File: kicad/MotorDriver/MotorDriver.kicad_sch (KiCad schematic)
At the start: 75 parts, among them J1 Conn_01x02_Socket, J2 Conn_01x03_Socket, U1 DRV8323RSRGZR, U2 CSD88599Q5DC, U3 CSD88599Q5DC, U5 CSD88599Q5DC, U6 STM32G474RETx

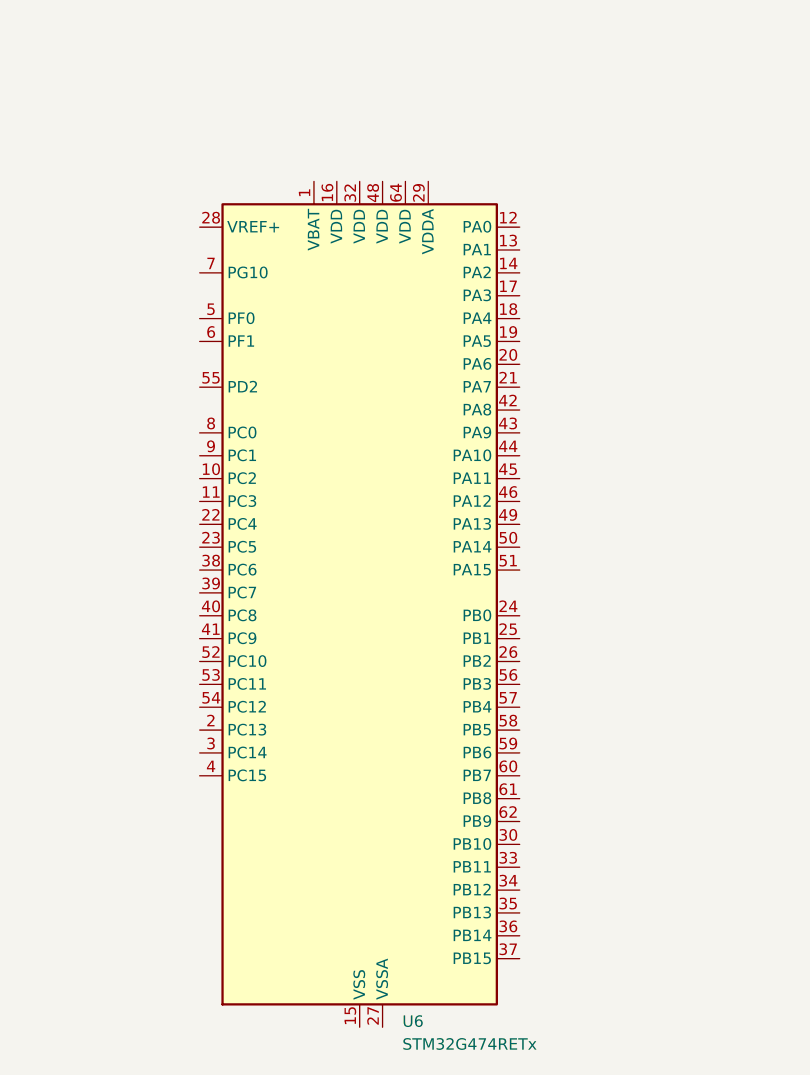
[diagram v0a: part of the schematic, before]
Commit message: Good progress on the leg prototype. Looking at the jacobian project again, i think I can use some stuff from that project to help size the link lengths and also something to relate the tip forces to joint torques
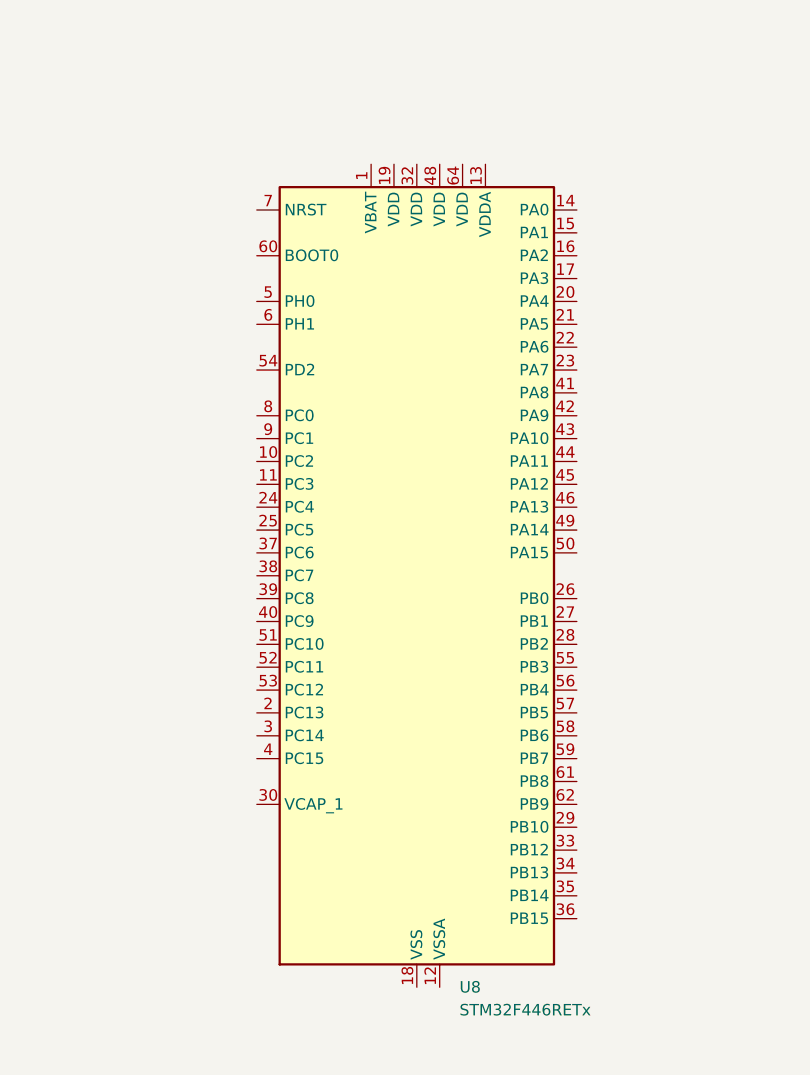
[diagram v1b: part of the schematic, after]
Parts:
- removed U6: STM32G474RETx, Package_QFP:LQFP-64_10x10mm_P0.5mm, symbol MCU_ST_STM32G4:STM32G474RETx
- added U8: STM32F446RETx, Package_QFP:LQFP-64_10x10mm_P0.5mm, symbol MCU_ST_STM32F4:STM32F446RETx
- L1: footprint (none) -> Inductor_SMD:L_0603_1608Metric
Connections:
- new net: U8.18 (VSS), U8.31 (VSS), U8.47 (VSS), U8.63 (VSS)
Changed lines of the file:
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@@
     (effects (font (size 1.27 1.27)) (justify left bottom))
+  )
+  (symbol (lib_id "MCU_ST_STM32F4:STM32F446RETx") (at 100.33 288.29 0) (unit 1)
+    (in_bom yes) (on_board yes) (dnp no) (fields_autoplaced)
+    (property "Reference" "U8" (at 105.0641 334.01 0)
+      (effects (font (size 1.27 1.27)) (justify left))
+    )
+    (property "Value" "STM32F446RETx" (at 105.0641 336.55 0)
+      (effects (font (size 1.27 1.27)) (justify left))
+    )
+    (property "Footprint" "Package_QFP:LQFP-64_10x10mm_P0.5mm" (at 85.09 331.47 0)
+      (effects (font (size 1.27 1.27)) (justify right) hide)
+    )
+    (property "Datasheet" "https://www.st.com/resource/en/datasheet/stm32f446re.pdf" (at 100.33 288.29 0)
+      (effects (font (size 1.27 1.27)) hide)
+    )
+    (pin "10")
+    (pin "30")
+    (pin "35")
+    (pin "2")
+    (pin "26")
+    (pin "23")
+    (pin "29")
+    (pin "27")
+    (pin "52")
+    (pin "31")
+    (pin "53")
+    (pin "58")
+    (pin "38")
+    (pin "19")
+    (pin "37")
+    (pin "28")
+    (pin "44")
+    (pin "50")
+    (pin "56")
+    (pin "59")
+    (pin "6")
+    (pin "12")
+    (pin "20")
+    (pin "36")
+    (pin "18")
+    (pin "49")
+    (pin "39")
+    (pin "55")
+    (pin "15")
+    (pin "16")
+    (pin "24")
+    (pin "34")
+    (pin "46")
+    (pin "51")
+    (pin "33")
+    (pin "54")
+    (pin "60")
+    (pin "1")
+    (pin "17")
+    (pin "42")
+    (pin "14")
+    (pin "43")
+    (pin "4")
+    (pin "5")
+    (pin "61")
+    (pin "62")
+    (pin "63")
+    (pin "11")
+    (pin "64")
+    (pin "7")
+    (pin "8")
+    (pin "9")
+    (pin "22")
+    (pin "21")
+    (pin "25")
+    (pin "13")
+    (pin "32")
+    (pin "45")
+    (pin "47")
+    (pin "48")
+    (pin "41")
+    (pin "3")
+    (pin "40")
+    (pin "57")
+    (instances
+      (project "MotorDriver"
+        (path "/1fa4c72f-b85f-4d78-9713-26aa572ca2e5"
+          (reference "U8") (unit 1)
+        )
+      )
+    )
   )
   (symbol (lib_id "power:Vdrive") (at 394.97 48.26 0) (unit 1)
@@
       (effects (font (size 1.27 1.27)))
     )
-    (property "Footprint" "" (at 148.59 113.665 0)
+    (property "Footprint" "Inductor_SMD:L_0603_1608Metric" (at 148.59 113.665 0)
       (effects (font (size 1.27 1.27)) hide)
     )
@@
         )
       )
-    )
-  )
-  (symbol (lib_id "MCU_ST_STM32G4:STM32G474RETx") (at 93.98 292.735 0) (unit 1)
-    (in_bom yes) (on_board yes) (dnp no) (fields_autoplaced)
-    (property "Reference" "U6" (at 98.7141 337.82 0)
-      (effects (font (size 1.27 1.27)) (justify left))
-    )
-    (property "Value" "STM32G474RETx" (at 98.7141 340.36 0)
-      (effects (font (size 1.27 1.27)) (justify left))
-    )
-    (property "Footprint" "Package_QFP:LQFP-64_10x10mm_P0.5mm" (at 78.74 335.915 0)
-      (effects (font (size 1.27 1.27)) (justify right) hide)
-    )
-    (property "Datasheet" "https://www.st.com/resource/en/datasheet/stm32g474re.pdf" (at 93.98 292.735 0)
-      (effects (font (size 1.27 1.27)) hide)
-    )
-    (pin "58")
-    (pin "21")
-    (pin "36")
-    (pin "42")
-    (pin "3")
-    (pin "23")
-    (pin "14")
-    (pin "31")
-    (pin "49")
-    (pin "5")
-    (pin "32")
-    (pin "15")
-    (pin "11")
-    (pin "30")
-    (pin "37")
-    (pin "55")
-    (pin "62")
-    (pin "48")
-    (pin "13")
-    (pin "2")
-    (pin "43")
-    (pin "56")
-    (pin "47")
-    (pin "50")
-    (pin "4")
-    (pin "10")
-    (pin "20")
-    (pin "17")
-    (pin "19")
-    (pin "22")
-    (pin "24")
-    (pin "26")
-    (pin "29")
-    (pin "34")
-    (pin "44")
-    (pin "45")
-    (pin "46")
-    (pin "53")
-    (pin "52")
-    (pin "57")
-    (pin "18")
-    (pin "12")
-    (pin "27")
-    (pin "61")
-    (pin "25")
-    (pin "39")
-    (pin "41")
-    (pin "6")
-    (pin "63")
-    (pin "64")
-    (pin "35")
-    (pin "1")
-    (pin "60")
-    (pin "33")
-    (pin "16")
-    (pin "40")
-    (pin "28")
-    (pin "38")
-    (pin "51")
-    (pin "54")
-    (pin "59")
-    (pin "7")
-    (pin "8")
-    (pin "9")
-    (instances
-      (project "MotorDriver"
-        (path "/1fa4c72f-b85f-4d78-9713-26aa572ca2e5"
-          (reference "U6") (unit 1)
-        )
-      )

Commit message: Schematic capture is like 80% complete. There are some components that don't have appropriate footprints, IE the 330 mH caps. Started board layout. I'm not sure if I can fit everything in the current board outline though. I may need to expand to a full circle instead of having the cutout sections.
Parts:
- removed C1, C11, C9: 0.01 uF, Capacitor_SMD:C_0603_1608Metric, symbol Device:C
- removed C10, C12, C2: 0.1 uF, Capacitor_SMD:C_0603_1608Metric, symbol Device:C
- removed C13: 2.2uF, Capacitor_SMD:C_0603_1608Metric, symbol Device:C
- removed C14, C7: 0.1uF, Capacitor_SMD:C_0603_1608Metric, symbol Device:C
- removed C15, C17, C18, C19, C20, C21, C22, C23: 1uF, Capacitor_SMD:C_0603_1608Metric, symbol Device:C
- removed C16: 0.047uF, Capacitor_SMD:C_0603_1608Metric, symbol Device:C
- removed C24: 22uF, Capacitor_SMD:C_0603_1608Metric, symbol Device:C
- removed C3, C4: 330uF, Capacitor_SMD:C_0603_1608Metric, symbol Device:C
- removed C5, C6, C8: 2200pF, Capacitor_SMD:C_0603_1608Metric, symbol Device:C
- removed D1, D2, D3: LED, LED_SMD:LED_0603_1608Metric, symbol Device:LED
- removed D4: 1N6857UR, Diode_SMD:D_MELF, symbol Diode:1N6857UR
- removed J1: Conn_01x02_Socket, Connector_PinHeader_2.54mm:PinHeader_1x02_P2.54mm_Vertical, symbol Connector:Conn_01x02_Socket
- removed J2: Conn_01x03_Socket, Connector_PinHeader_2.54mm:PinHeader_1x03_P2.54mm_Vertical, symbol Connector:Conn_01x03_Socket
- removed L1: L, Inductor_SMD:L_0603_1608Metric, symbol Device:L
- removed NT1, NT10, NT2, NT3, NT4, NT5, NT6, NT7, NT8, NT9: NetTie_2, NetTie:NetTie-2_SMD_Pad0.5mm, symbol Device:NetTie_2
- removed R1, R12, R4, R9: 82.0k, Resistor_SMD:R_0603_1608Metric, symbol Device:R
- removed R10, R13, R2, R5: 4.99k, Resistor_SMD:R_0603_1608Metric, symbol Device:R
- removed R11, R14, R3: 0.007, Resistor_SMD:R_0603_1608Metric, symbol Device:R
- removed R15: 330, Resistor_SMD:R_0603_1608Metric, symbol Device:R
- removed R16: 10k, Resistor_SMD:R_0603_1608Metric, symbol Device:R
- removed R17: 28.0k, Resistor_SMD:R_0603_1608Metric, symbol Device:R
- removed R18: 8.45k, Resistor_SMD:R_0603_1608Metric, symbol Device:R
- removed R6, R7, R8: 56, Resistor_SMD:R_0603_1608Metric, symbol Device:R
- removed TP1, TP2, TP3, TP4, TP5, TP6, TP7, TP8, TP9: TestPoint, TestPoint:TestPoint_Pad_D2.5mm, symbol Connector:TestPoint
- removed U1: DRV8323RSRGZR, TylerLib:QFN50P700X700X100-49N, symbol TylerLib:DRV8323RSRGZR
- removed U2, U3, U5: CSD88599Q5DC, TylerLib:MOSFET_CSD88599Q5DC, symbol TylerLib:CSD88599Q5DC
- removed U4: ~, TylerLib:SOT65P210X110-6N, symbol TylerLib:SOT65P210X110-6N
- removed U7: ~, Package_SO:TSSOP-14_4.4x5mm_P0.65mm, symbol TylerLib:AS5147U-HTSM
- removed U8: STM32F446RETx, Package_QFP:LQFP-64_10x10mm_P0.5mm, symbol MCU_ST_STM32F4:STM32F446RETx
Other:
- added sheet Encoder (AS5147U.kicad_sch)
- added sheet Microcontroller (stm32f446.kicad_sch)
- added sheet MotorController (DRV8323RS.kicad_sch)
- note removed: "HALF-BRIDGES & SENSE"
- note removed: "Low pass filters Place near BP headers"
- note removed: "Voltage Protection"

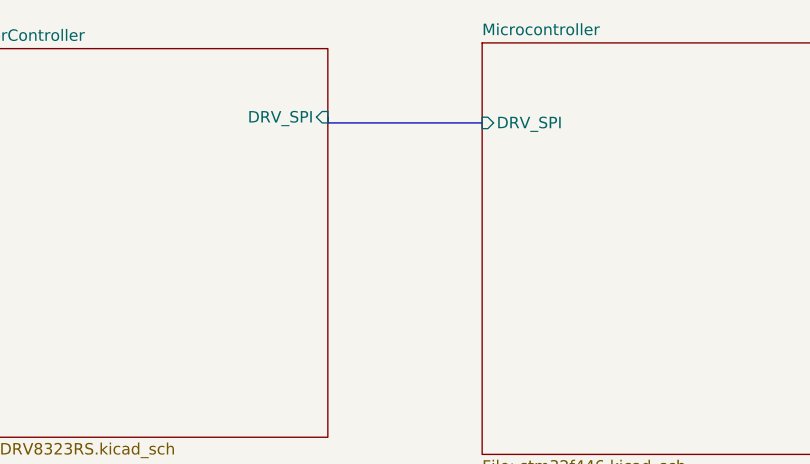
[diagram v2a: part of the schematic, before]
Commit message: Updated the planetary gearbox design. It is much better with retaining rings and bearing support. 95% done with the PCB routing. Need to just do a final routing check and i think I can put the order in
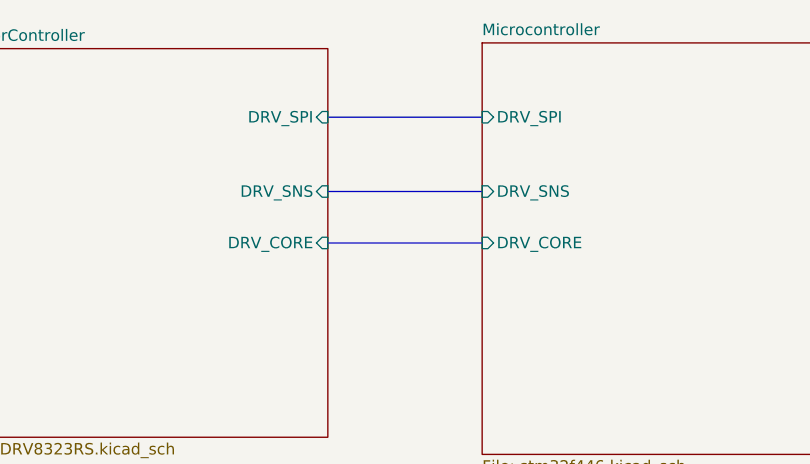
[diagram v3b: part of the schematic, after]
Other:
- sheet Microcontroller ports: added DRV_CORE, DRV_SNS; removed none
- sheet MotorController ports: added DRV_CORE, DRV_SNS; removed none
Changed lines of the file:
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@@
 (kicad_sch (version 20230121) (generator eeschema)
   (paper "A4")
-  (bus (pts (xy 160.655 90.805) (xy 175.26 90.805))
+  (bus (pts (xy 96.52 86.36) (xy 113.665 86.36))
     (stroke (width 0) (type default))
   )
-  (bus (pts (xy 96.52 86.36) (xy 96.52 86.995))
+  (bus (pts (xy 160.655 90.805) (xy 175.26 90.805))
     (stroke (width 0) (type default))
   )
@@
     (stroke (width 0) (type default))
   )
-  (bus (pts (xy 96.52 86.995) (xy 113.665 86.995))
+  (bus (pts (xy 96.52 100.33) (xy 113.665 100.33))
+    (stroke (width 0) (type default))
+  )
+  (bus (pts (xy 96.52 94.615) (xy 113.665 94.615))
     (stroke (width 0) (type default))
   )
@@
       (effects (font (size 1.27 1.27)) (justify left top))
     )
-    (pin "DRV_SPI" input (at 113.665 86.995 180)
+    (pin "DRV_SPI" input (at 113.665 86.36 180)
       (effects (font (size 1.27 1.27)) (justify left))
     )
@@
     (pin "ENC_SIG" input (at 160.655 90.805 0)
       (effects (font (size 1.27 1.27)) (justify right))
+    )
+    (pin "DRV_CORE" input (at 113.665 100.33 180)
+      (effects (font (size 1.27 1.27)) (justify left))
+    )
+    (pin "DRV_SNS" input (at 113.665 94.615 180)
+      (effects (font (size 1.27 1.27)) (justify left))
     )
     (instances
@@
       (effects (font (size 1.27 1.27)) (justify right))
     )
+    (pin "DRV_SNS" input (at 96.52 94.615 0)
+      (effects (font (size 1.27 1.27)) (justify right))
+    )
+    (pin "DRV_CORE" input (at 96.52 100.33 0)
+      (effects (font (size 1.27 1.27)) (justify right))
+    )
